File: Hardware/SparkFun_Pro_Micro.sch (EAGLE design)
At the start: 33 parts, among them J1 USB-A-H, U2 MIC5219, U3 ATMEGA32U4, Y1 16MHz

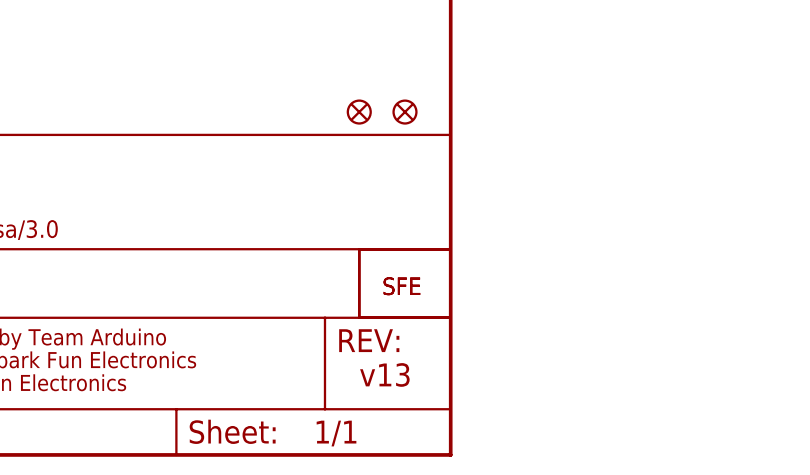
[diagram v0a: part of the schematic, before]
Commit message: Remove SparkFun logo on bottom silkscreen
This is cleverly hiding in the corner of the schematic as part of the title frame (look for "SFE" on the right).
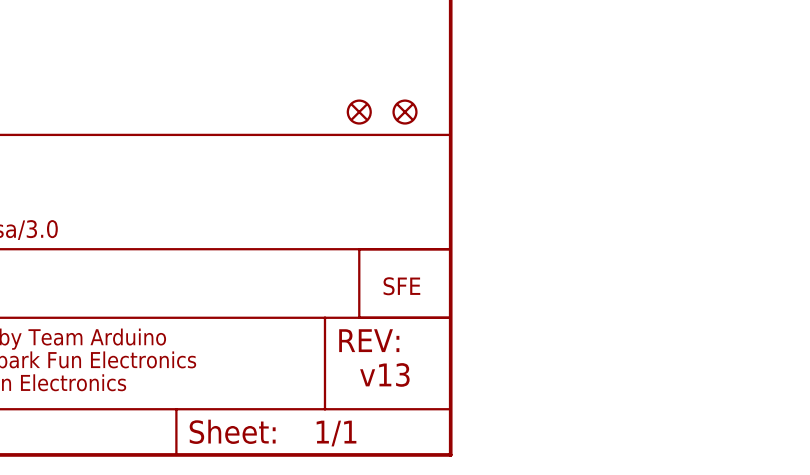
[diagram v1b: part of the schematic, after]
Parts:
- removed U$11: LOGO-SFENEW, SparkFun:LOGO-SFENEW
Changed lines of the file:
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@@
 <part name="R6" library="SparkFun" deviceset="RESISTOR" device="0603-RES" value="330"/>
 <part name="D3" library="SparkFun" deviceset="LED" device="0603" value="Green"/>
-<part name="U$11" library="SparkFun" deviceset="LOGO-SFE" device="NEW"/>
 <part name="U2" library="SparkFun" deviceset="V_REG_LDO" device="SMD" value="MIC5219"/>
 <part name="C19" library="SparkFun" deviceset="CAP_POL" device="1206" value="10uF"/>
@@
 <attribute name="VALUE" x="196.977" y="68.326" size="1.778" layer="96" rot="R270"/>
 </instance>
-<instance part="U$11" gate="G$1" x="241.3" y="17.78"/>
 <instance part="U2" gate="G$1" x="63.5" y="154.94"/>
 <instance part="C19" gate="G$1" x="40.64" y="154.94"/>

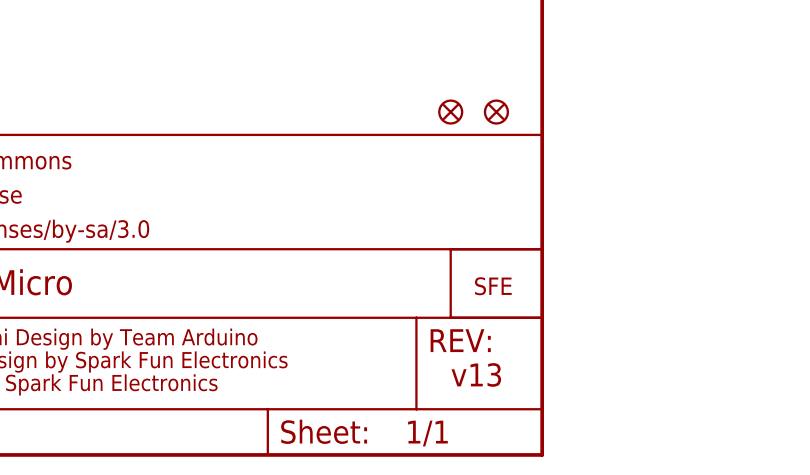
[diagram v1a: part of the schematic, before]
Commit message: Add PartsNotIncluded logo to bottom silkscreen
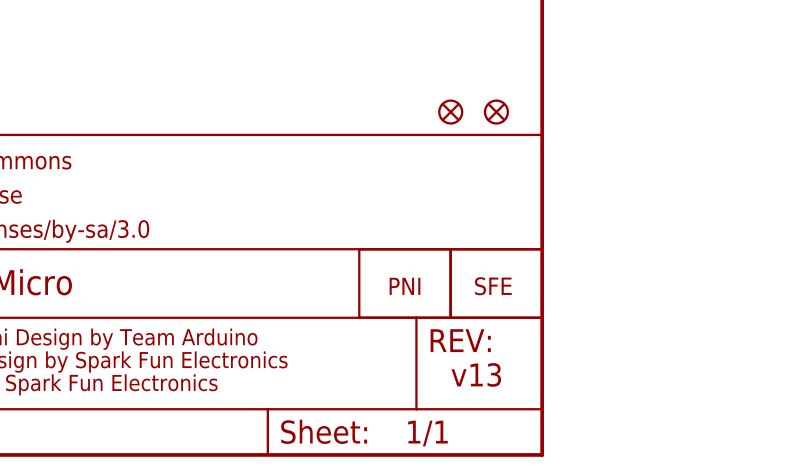
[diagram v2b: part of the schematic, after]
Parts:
- added U$2: PNI-PRO-MICRO-SPLIT-LOGO-TEXT, PartsNotIncluded:PNI-PRO-MICRO-SPLIT-LOGO-TEXT
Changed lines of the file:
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@@
 <part name="P+2" library="SparkFun" deviceset="VCC" device=""/>
 <part name="J1" library="SparkFun-Connectors" deviceset="USB" device="-A-H"/>
+<part name="U$2" library="PartsNotIncluded" deviceset="PNI-PRO-MICRO-SPLIT-LOGO-TEXT" device=""/>
 </parts>
 <sheets>
@@
 <instance part="P+2" gate="1" x="210.82" y="60.96" rot="R180"/>
 <instance part="J1" gate="G$1" x="104.14" y="91.44" rot="R180"/>
+<instance part="U$2" gate="G$1" x="231.14" y="17.78"/>
 </instances>
 <busses>

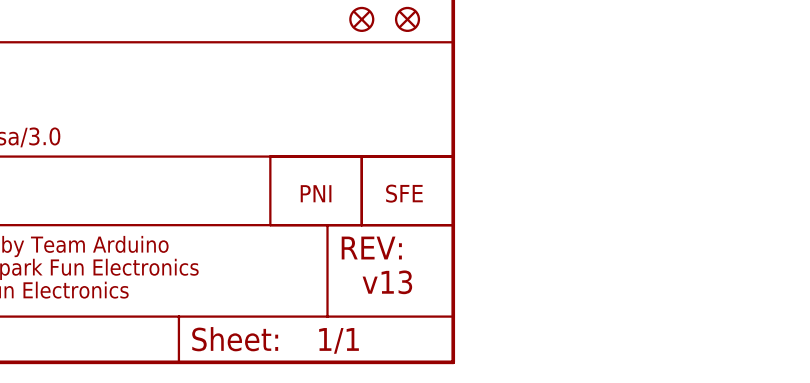
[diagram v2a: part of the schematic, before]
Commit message: Update version number in schematic (v1.1)
Using the USB-A version number instead of the Pro Micro number, for internal consistency
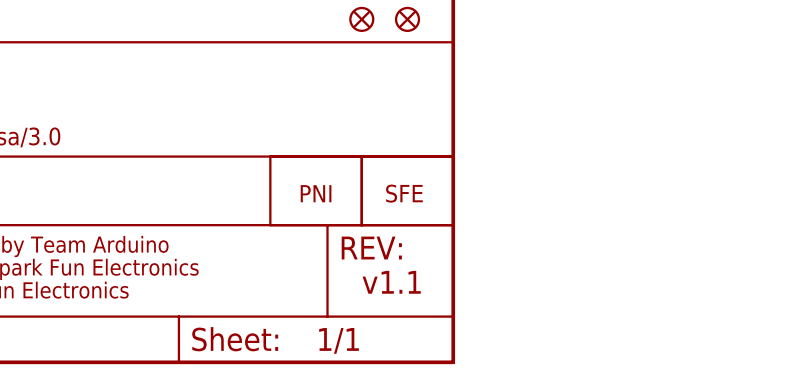
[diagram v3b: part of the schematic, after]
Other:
- note added: "v1.1"
- note removed: "v13"
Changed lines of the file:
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@@
 <text x="251.46" y="147.32" size="1.778" layer="97">Routed directly inward or outward from each leg on the IC</text>
 <text x="251.46" y="144.78" size="1.778" layer="97">Added two small squares of tRestrict to keep the ground plane away from the sides of IC legs</text>
-<text x="238.76" y="7.62" size="2.54" layer="94">v13</text>
+<text x="238.76" y="7.62" size="2.54" layer="94">v1.1</text>
 </plain>
 <instances>

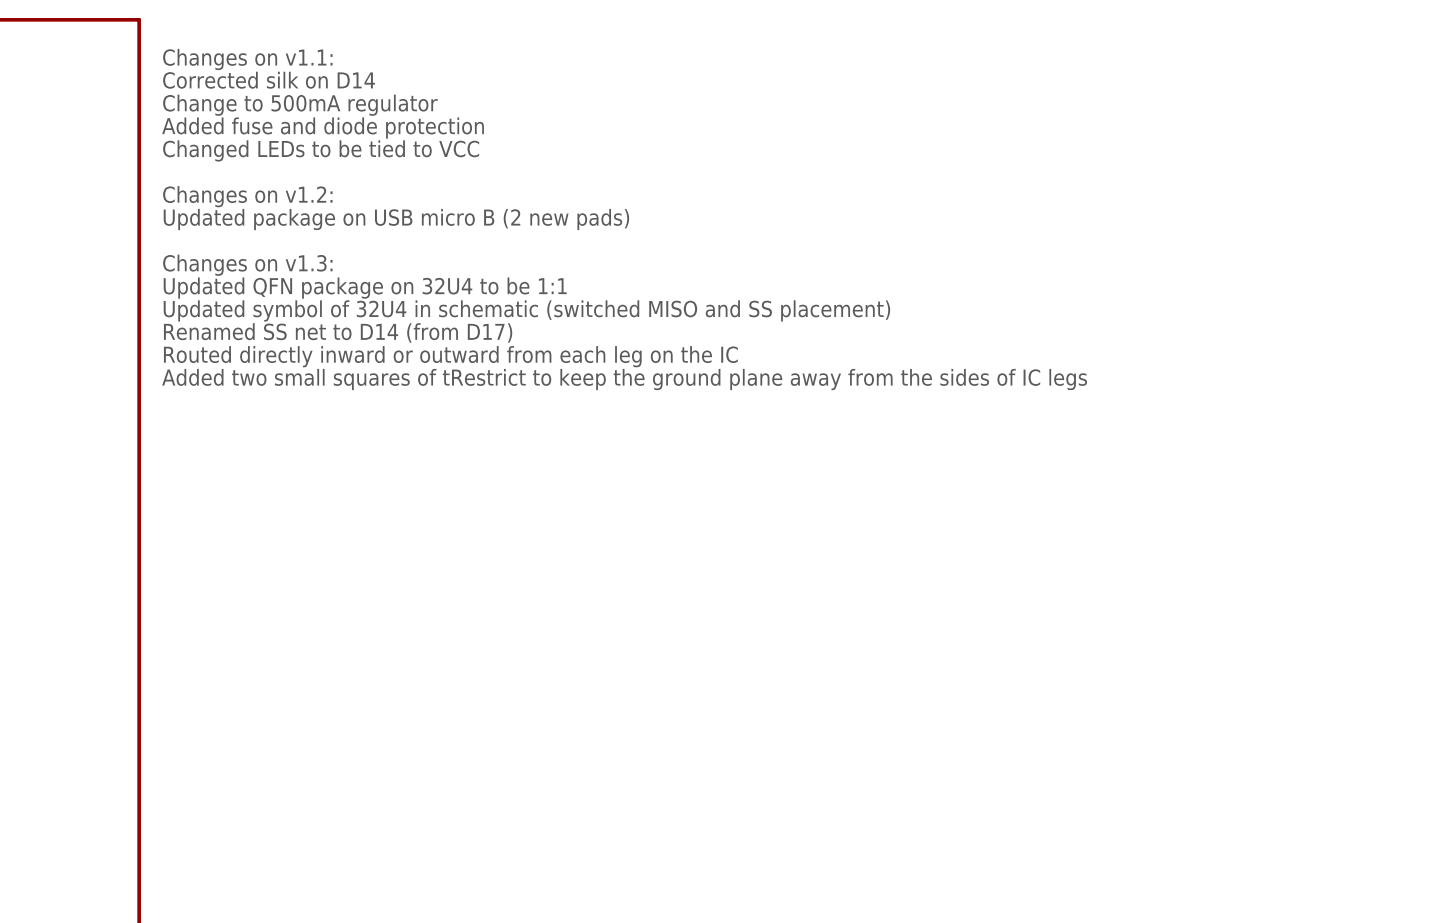
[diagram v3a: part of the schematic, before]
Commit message: Add USB-A version changes to schematic
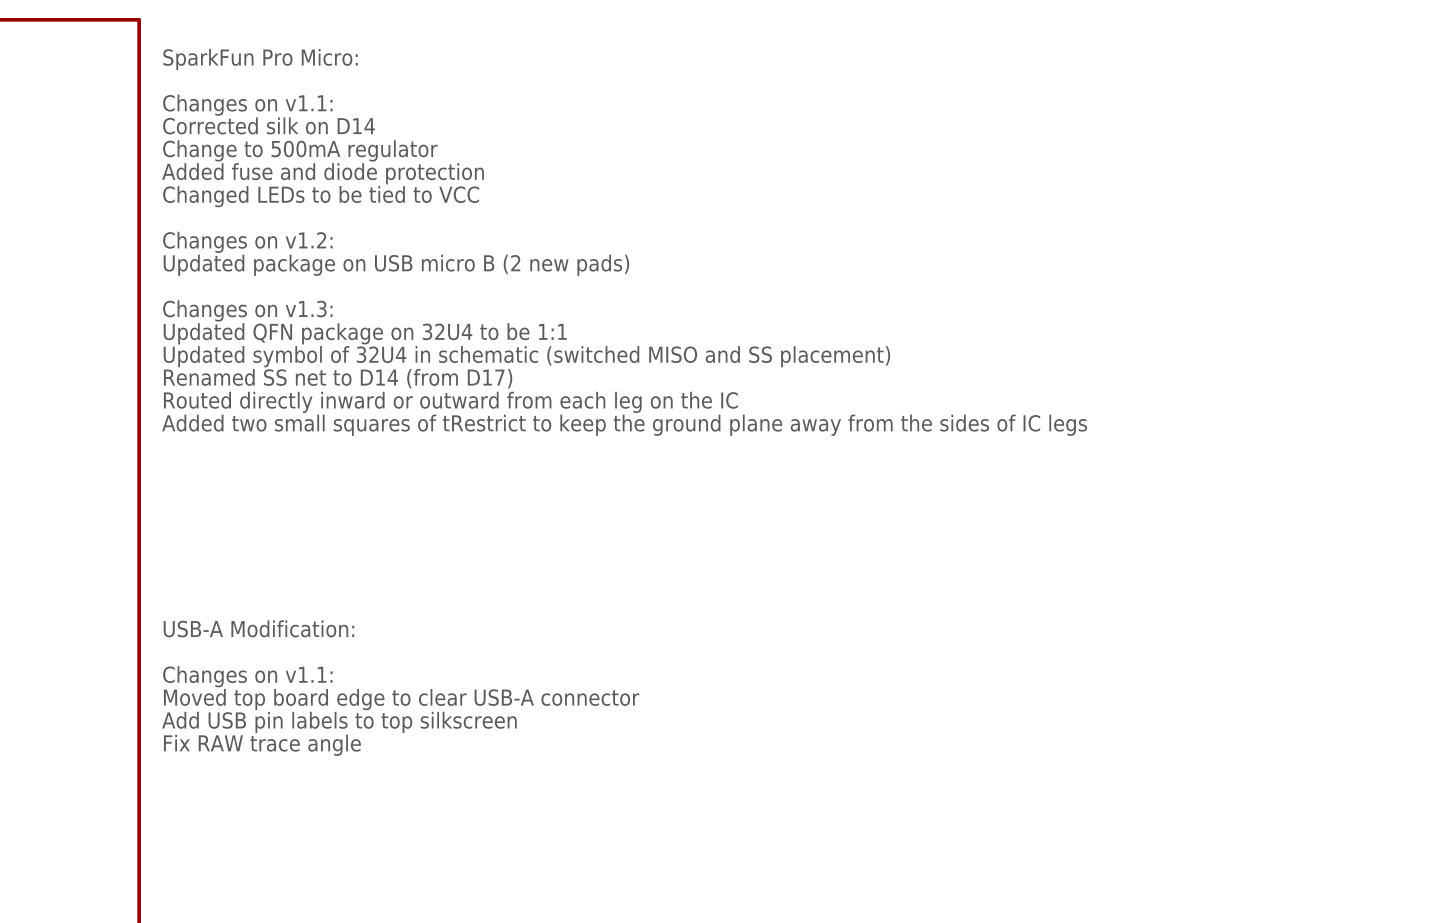
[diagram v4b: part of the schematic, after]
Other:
- note added: "Add USB pin labels to top silkscreen"
- note added: "Fix RAW trace angle"
- note added: "Moved top board edge to clear USB-A connector"
- note added: "SparkFun Pro Micro:"
- note added: "USB-A Modification:"
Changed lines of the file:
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@@
 <text x="218.44" y="147.32" size="1.778" layer="91">Not used</text>
 <text x="166.624" y="7.112" size="1.778" layer="94">Pro Micro Design by Spark Fun Electronics</text>
-<text x="251.46" y="180.34" size="1.778" layer="97">Changes on v1.1:</text>
-<text x="251.46" y="177.8" size="1.778" layer="97">Corrected silk on D14</text>
-<text x="251.46" y="175.26" size="1.778" layer="97">Change to 500mA regulator</text>
+<text x="251.46" y="175.26" size="1.778" layer="97">Changes on v1.1:</text>
+<text x="251.46" y="172.72" size="1.778" layer="97">Corrected silk on D14</text>
+<text x="251.46" y="170.18" size="1.778" layer="97">Change to 500mA regulator</text>
 <text x="48.26" y="167.64" size="1.778" layer="97">Open for 3.3V Board</text>
-<text x="251.46" y="172.72" size="1.778" layer="97">Added fuse and diode protection</text>
-<text x="251.46" y="170.18" size="1.778" layer="97">Changed LEDs to be tied to VCC</text>
-<text x="251.46" y="165.1" size="1.778" layer="97">Changes on v1.2:</text>
-<text x="251.46" y="162.56" size="1.778" layer="97">Updated package on USB micro B (2 new pads)</text>
-<text x="251.46" y="157.48" size="1.778" layer="97">Changes on v1.3:</text>
-<text x="251.46" y="154.94" size="1.778" layer="97">Updated QFN package on 32U4 to be 1:1</text>
-<text x="251.46" y="152.4" size="1.778" layer="97">Updated symbol of 32U4 in schematic (switched MISO and SS placement)</text>
-<text x="251.46" y="149.86" size="1.778" layer="97">Renamed SS net to D14 (from D17)</text>
-<text x="251.46" y="147.32" size="1.778" layer="97">Routed directly inward or outward from each leg on the IC</text>
-<text x="251.46" y="144.78" size="1.778" layer="97">Added two small squares of tRestrict to keep the ground plane away from the sides of IC legs</text>
+<text x="251.46" y="167.64" size="1.778" layer="97">Added fuse and diode protection</text>
+<text x="251.46" y="165.1" size="1.778" layer="97">Changed LEDs to be tied to VCC</text>
+<text x="251.46" y="160.02" size="1.778" layer="97">Changes on v1.2:</text>
+<text x="251.46" y="157.48" size="1.778" layer="97">Updated package on USB micro B (2 new pads)</text>
+<text x="251.46" y="152.4" size="1.778" layer="97">Changes on v1.3:</text>
+<text x="251.46" y="149.86" size="1.778" layer="97">Updated QFN package on 32U4 to be 1:1</text>
+<text x="251.46" y="147.32" size="1.778" layer="97">Updated symbol of 32U4 in schematic (switched MISO and SS placement)</text>
+<text x="251.46" y="144.78" size="1.778" layer="97">Renamed SS net to D14 (from D17)</text>
+<text x="251.46" y="142.24" size="1.778" layer="97">Routed directly inward or outward from each leg on the IC</text>
+<text x="251.46" y="139.7" size="1.778" layer="97">Added two small squares of tRestrict to keep the ground plane away from the sides of IC legs</text>
 <text x="238.76" y="7.62" size="2.54" layer="94">v1.1</text>
+<text x="251.46" y="180.34" size="1.778" layer="97">SparkFun Pro Micro:</text>
+<text x="251.46" y="111.76" size="1.778" layer="97">Changes on v1.1:</text>
+<text x="251.46" y="109.22" size="1.778" layer="97">Moved top board edge to clear USB-A connector</text>
+<text x="251.46" y="106.68" size="1.778" layer="97">Add USB pin labels to top silkscreen</text>
+<text x="251.46" y="104.14" size="1.778" layer="97">Fix RAW trace angle</text>
+<text x="251.46" y="116.84" size="1.778" layer="97">USB-A Modification:</text>
 </plain>
 <instances>
